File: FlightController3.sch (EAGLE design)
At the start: 27 parts, among them U1 NUCLEO_L432KC

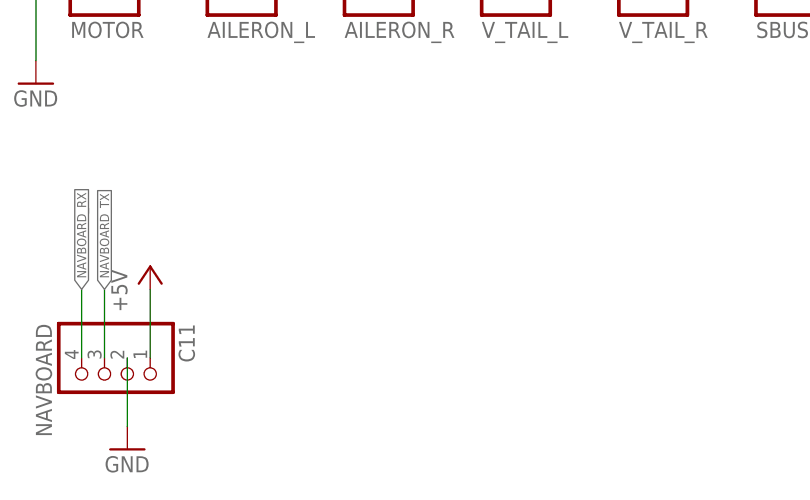
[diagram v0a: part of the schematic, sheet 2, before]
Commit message: added reset header
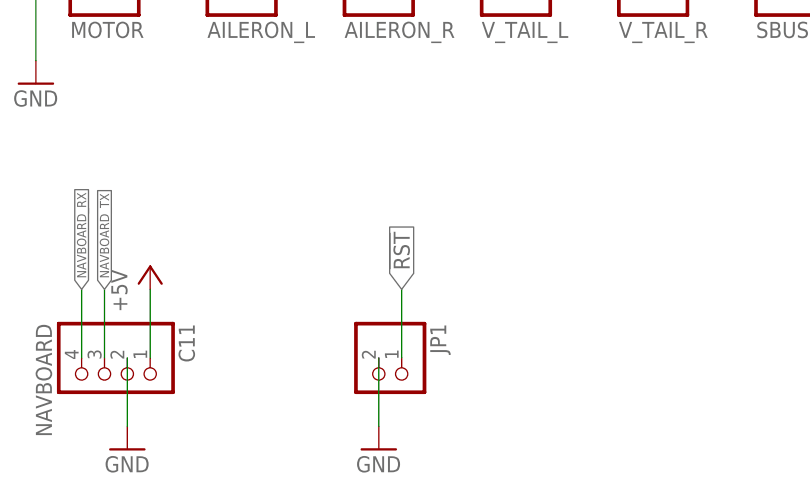
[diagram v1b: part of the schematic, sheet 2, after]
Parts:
- added JP1: (no value), pinhead:PINHD-1X2
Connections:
- new net !RST: JP1.1, U1.!RST
- net GND: now also JP1.2
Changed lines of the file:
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@@
 <part name="FRAME4" library="frames" deviceset="A4L-LOC" device=""/>
 <part name="U$1" library="toolbox" deviceset="TOOLBOX_LOGO" device=""/>
+<part name="JP1" library="pinhead" deviceset="PINHD-1X2" device=""/>
+<part name="GND8" library="supply1" deviceset="GND" device=""/>
 </parts>
 <sheets>
@@
 <wire x1="111.76" y1="116.84" x2="106.68" y2="116.84" width="0.1524" layer="91"/>
 <label x="106.68" y="116.84" size="1.778" layer="95" rot="R180" xref="yes"/>
+</segment>
+</net>
+<net name="!RST" class="0">
+<segment>
+<pinref part="U1" gate="G$1" pin="!RST"/>
+<wire x1="147.32" y1="76.2" x2="152.4" y2="76.2" width="0.1524" layer="91"/>
+<label x="152.4" y="76.2" size="1.778" layer="95" xref="yes"/>
 </segment>
 </net>
@@
 <instance part="C14" gate="A" x="218.44" y="114.3" rot="R270"/>
 <instance part="FRAME1" gate="G$1" x="0" y="0"/>
+<instance part="JP1" gate="G$1" x="58.42" y="81.28" rot="R270"/>
+<instance part="GND8" gate="1" x="58.42" y="73.66"/>
 </instances>
 <busses>
@@
 <junction x="220.98" y="129.54"/>
 </segment>
+<segment>
+<pinref part="JP1" gate="G$1" pin="2"/>
+<wire x1="58.42" y1="83.82" x2="58.42" y2="76.2" width="0.1524" layer="91"/>
+<pinref part="GND8" gate="1" pin="GND"/>
+</segment>
 </net>
 <net name="PPM_MOTOR" class="0">
@@
 </segment>
 </net>
+<net name="!RST" class="0">
+<segment>
+<pinref part="JP1" gate="G$1" pin="1"/>
+<wire x1="60.96" y1="83.82" x2="60.96" y2="91.44" width="0.1524" layer="91"/>
+<label x="60.96" y="91.44" size="1.778" layer="95" rot="R90" xref="yes"/>
+</segment>
+</net>

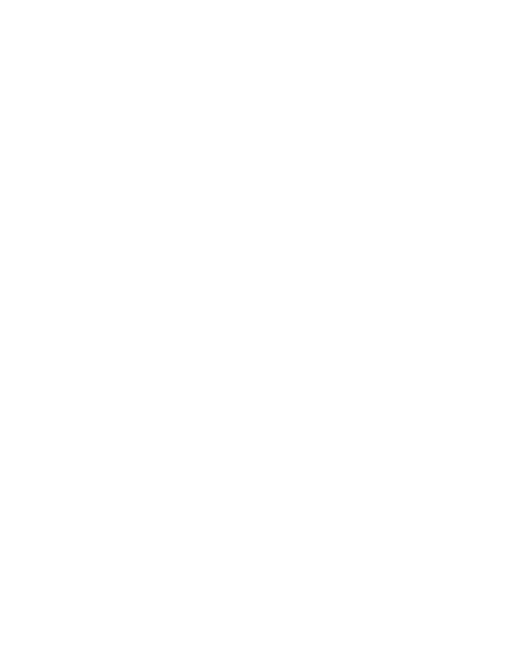
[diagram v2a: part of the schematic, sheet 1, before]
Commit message: power LEDs
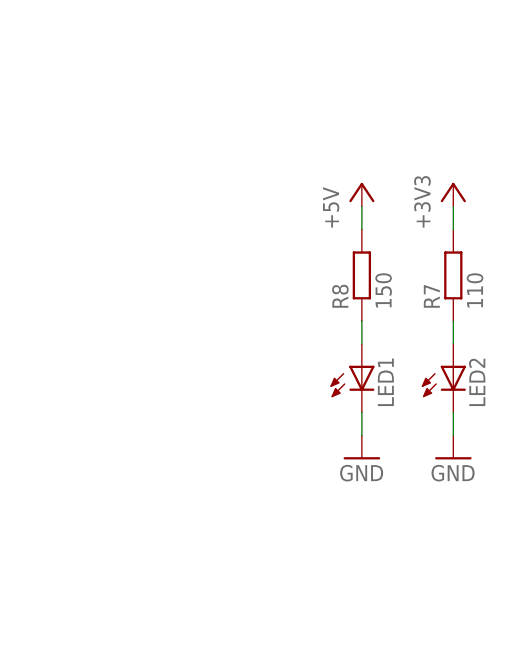
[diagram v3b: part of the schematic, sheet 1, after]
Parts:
- added LED1, LED2: (no value), led:LEDSML0603
- added R7: 110, resistor:R-EU_M1206
- added R8: 150, resistor:R-EU_M1206
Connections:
- new net N$2: LED2.A, R7.1
- new net N$3: LED1.A, R8.1
- net +3V3: now also R7.2
- net +5V: now also R8.2
- net GND: now also LED1.C, LED2.C
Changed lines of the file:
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@@
 <part name="JP1" library="pinhead" deviceset="PINHD-1X2" device=""/>
 <part name="GND8" library="supply1" deviceset="GND" device=""/>
+<part name="LED1" library="led" deviceset="LED" device="SML0603"/>
+<part name="LED2" library="led" deviceset="LED" device="SML0603"/>
+<part name="+3V2" library="supply1" deviceset="+3V3" device=""/>
+<part name="P+8" library="supply1" deviceset="+5V" device=""/>
+<part name="R7" library="resistor" deviceset="R-EU_" device="M1206" value="110"/>
+<part name="R8" library="resistor" deviceset="R-EU_" device="M1206" value="150"/>
+<part name="GND9" library="supply1" deviceset="GND" device=""/>
+<part name="GND10" library="supply1" deviceset="GND" device=""/>
 </parts>
 <sheets>
@@
 <instance part="FRAME2" gate="G$1" x="0" y="0"/>
 <instance part="U$1" gate="G$1" x="35.56" y="154.94"/>
+<instance part="LED1" gate="G$1" x="223.52" y="111.76"/>
+<instance part="LED2" gate="G$1" x="233.68" y="111.76"/>
+<instance part="+3V2" gate="G$1" x="233.68" y="132.08"/>
+<instance part="P+8" gate="1" x="223.52" y="132.08"/>
+<instance part="R7" gate="G$1" x="233.68" y="121.92" rot="R90"/>
+<instance part="R8" gate="G$1" x="223.52" y="121.92" rot="R90"/>
+<instance part="GND9" gate="1" x="223.52" y="101.6"/>
+<instance part="GND10" gate="1" x="233.68" y="101.6"/>
 </instances>
 <busses>
@@
 <pinref part="P+3" gate="1" pin="+5V"/>
 </segment>
+<segment>
+<pinref part="P+8" gate="1" pin="+5V"/>
+<pinref part="R8" gate="G$1" pin="2"/>
+<wire x1="223.52" y1="129.54" x2="223.52" y2="127" width="0.1524" layer="91"/>
+</segment>
 </net>
 <net name="GND" class="0">
@@
 <wire x1="104.14" y1="76.2" x2="104.14" y2="68.58" width="0.1524" layer="91"/>
 <pinref part="GND4" gate="1" pin="GND"/>
+</segment>
+<segment>
+<pinref part="LED2" gate="G$1" pin="C"/>
+<pinref part="GND10" gate="1" pin="GND"/>
+<wire x1="233.68" y1="106.68" x2="233.68" y2="104.14" width="0.1524" layer="91"/>
+</segment>
+<segment>
+<pinref part="LED1" gate="G$1" pin="C"/>
+<pinref part="GND9" gate="1" pin="GND"/>
+<wire x1="223.52" y1="106.68" x2="223.52" y2="104.14" width="0.1524" layer="91"/>
 </segment>
 </net>
@@
 <wire x1="162.56" y1="86.36" x2="162.56" y2="93.98" width="0.1524" layer="91"/>
 <pinref part="+3V1" gate="G$1" pin="+3V3"/>
+</segment>
+<segment>
+<pinref part="+3V2" gate="G$1" pin="+3V3"/>
+<pinref part="R7" gate="G$1" pin="2"/>
+<wire x1="233.68" y1="129.54" x2="233.68" y2="127" width="0.1524" layer="91"/>
 </segment>
 </net>
@@
 </segment>
 </net>
+<net name="N$2" class="0">
+<segment>
+<pinref part="R7" gate="G$1" pin="1"/>
+<pinref part="LED2" gate="G$1" pin="A"/>
+<wire x1="233.68" y1="116.84" x2="233.68" y2="114.3" width="0.1524" layer="91"/>
+</segment>
+</net>
+<net name="N$3" class="0">
+<segment>
+<pinref part="LED1" gate="G$1" pin="A"/>
+<pinref part="R8" gate="G$1" pin="1"/>
+<wire x1="223.52" y1="114.3" x2="223.52" y2="116.84" width="0.1524" layer="91"/>
+</segment>
+</net>

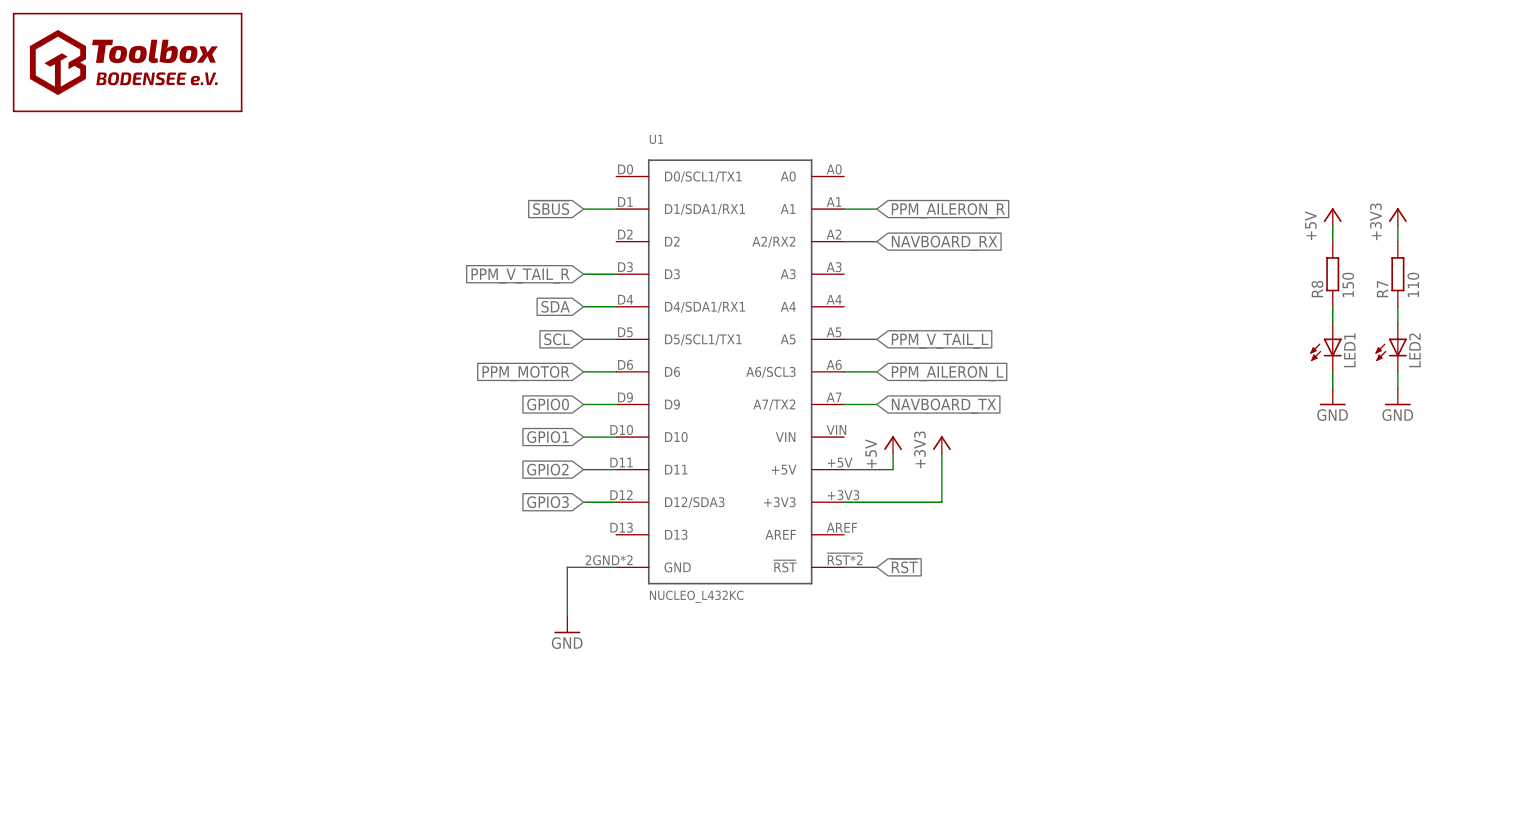
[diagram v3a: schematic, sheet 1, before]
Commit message: capacitors, dimensions, reset button
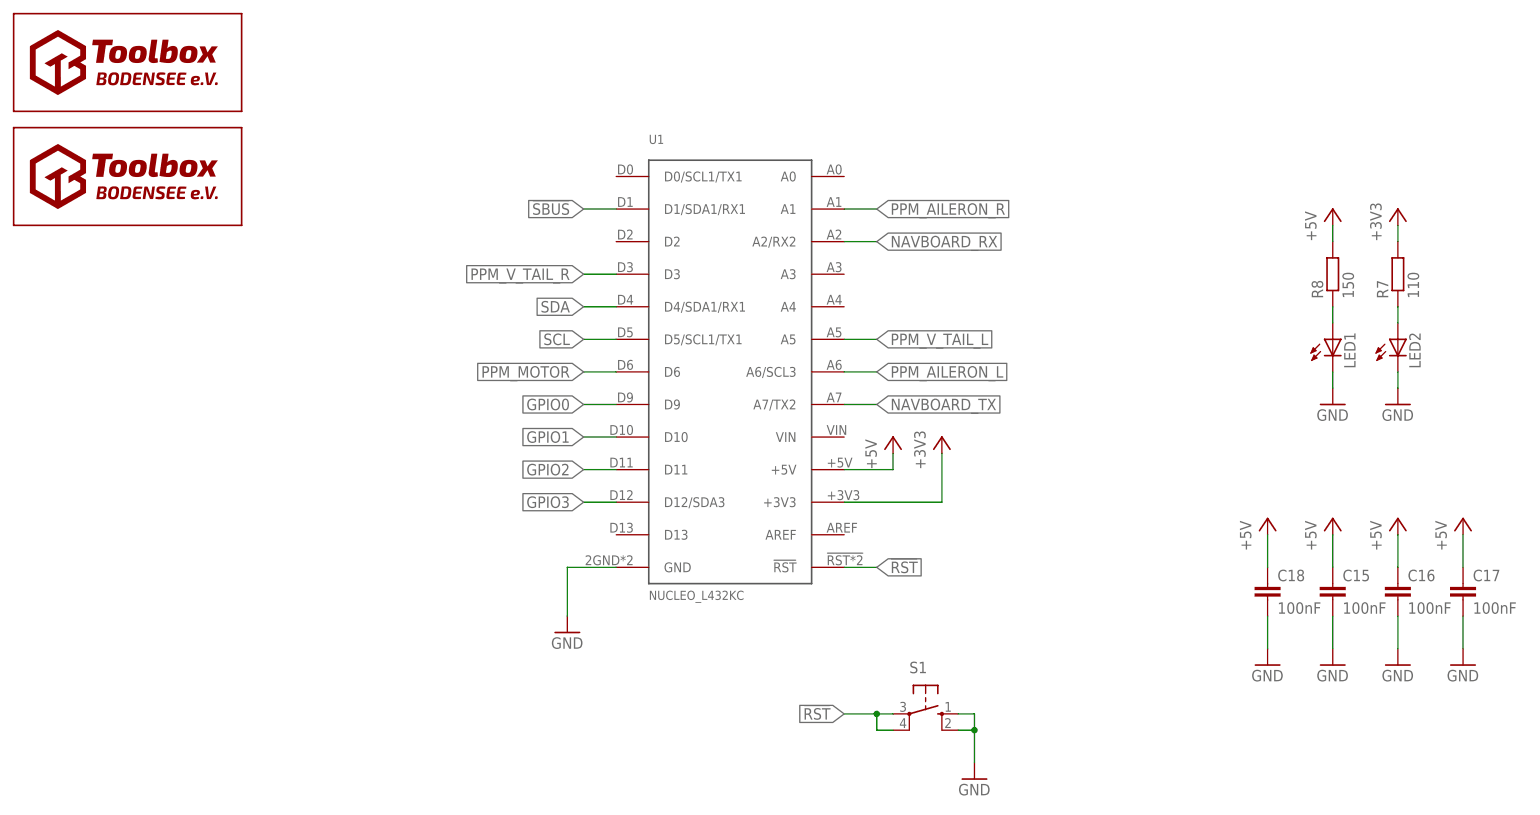
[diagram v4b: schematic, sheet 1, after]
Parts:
- added C15, C16, C17, C18: 100nF, resistor:C-EUC1206
- added S1: (no value), switch-omron:10-XX
- added U$2: TOOLBOX_LOGO, toolbox:TOOLBOX_LOGO
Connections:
- net !RST: now also S1.P, S1.P1
- net +5V: now also C15.1, C16.1, C17.1, C18.1
- net GND: now also C15.2, C16.2, C17.2, C18.2, S1.S, S1.S1
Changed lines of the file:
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@@
 <part name="GND9" library="supply1" deviceset="GND" device=""/>
 <part name="GND10" library="supply1" deviceset="GND" device=""/>
+<part name="C15" library="resistor" deviceset="C-EU" device="C1206" value="100nF"/>
+<part name="C16" library="resistor" deviceset="C-EU" device="C1206" value="100nF"/>
+<part name="C17" library="resistor" deviceset="C-EU" device="C1206" value="100nF"/>
+<part name="C18" library="resistor" deviceset="C-EU" device="C1206" value="100nF"/>
+<part name="P+10" library="supply1" deviceset="+5V" device=""/>
+<part name="P+11" library="supply1" deviceset="+5V" device=""/>
+<part name="P+12" library="supply1" deviceset="+5V" device=""/>
+<part name="P+13" library="supply1" deviceset="+5V" device=""/>
+<part name="GND12" library="supply1" deviceset="GND" device=""/>
+<part name="GND13" library="supply1" deviceset="GND" device=""/>
+<part name="GND14" library="supply1" deviceset="GND" device=""/>
+<part name="GND15" library="supply1" deviceset="GND" device=""/>
+<part name="S1" library="switch-omron" deviceset="10-XX" device=""/>
+<part name="GND11" library="supply1" deviceset="GND" device=""/>
+<part name="U$2" library="toolbox" deviceset="TOOLBOX_LOGO" device=""/>
 </parts>
 <sheets>
@@
 <instance part="GND9" gate="1" x="223.52" y="101.6"/>
 <instance part="GND10" gate="1" x="233.68" y="101.6"/>
+<instance part="C15" gate="G$1" x="223.52" y="73.66"/>
+<instance part="C16" gate="G$1" x="233.68" y="73.66"/>
+<instance part="C17" gate="G$1" x="243.84" y="73.66"/>
+<instance part="C18" gate="G$1" x="213.36" y="73.66"/>
+<instance part="P+10" gate="1" x="213.36" y="83.82"/>
+<instance part="P+11" gate="1" x="223.52" y="83.82"/>
+<instance part="P+12" gate="1" x="233.68" y="83.82"/>
+<instance part="P+13" gate="1" x="243.84" y="83.82"/>
+<instance part="GND12" gate="1" x="213.36" y="60.96"/>
+<instance part="GND13" gate="1" x="223.52" y="60.96"/>
+<instance part="GND14" gate="1" x="233.68" y="60.96"/>
+<instance part="GND15" gate="1" x="243.84" y="60.96"/>
+<instance part="S1" gate="1" x="160.02" y="53.34" rot="R270"/>
+<instance part="GND11" gate="1" x="167.64" y="43.18"/>
+<instance part="U$2" gate="G$1" x="35.56" y="137.16"/>
 </instances>
 <busses>
@@
 <wire x1="223.52" y1="129.54" x2="223.52" y2="127" width="0.1524" layer="91"/>
 </segment>
+<segment>
+<pinref part="P+10" gate="1" pin="+5V"/>
+<pinref part="C18" gate="G$1" pin="1"/>
+<wire x1="213.36" y1="81.28" x2="213.36" y2="76.2" width="0.1524" layer="91"/>
+</segment>
+<segment>
+<pinref part="C15" gate="G$1" pin="1"/>
+<pinref part="P+11" gate="1" pin="+5V"/>
+<wire x1="223.52" y1="76.2" x2="223.52" y2="81.28" width="0.1524" layer="91"/>
+</segment>
+<segment>
+<pinref part="P+12" gate="1" pin="+5V"/>
+<pinref part="C16" gate="G$1" pin="1"/>
+<wire x1="233.68" y1="81.28" x2="233.68" y2="76.2" width="0.1524" layer="91"/>
+</segment>
+<segment>
+<pinref part="C17" gate="G$1" pin="1"/>
+<pinref part="P+13" gate="1" pin="+5V"/>
+<wire x1="243.84" y1="76.2" x2="243.84" y2="81.28" width="0.1524" layer="91"/>
+</segment>
 </net>
 <net name="GND" class="0">
@@
 <wire x1="223.52" y1="106.68" x2="223.52" y2="104.14" width="0.1524" layer="91"/>
 </segment>
+<segment>
+<pinref part="C17" gate="G$1" pin="2"/>
+<pinref part="GND15" gate="1" pin="GND"/>
+<wire x1="243.84" y1="68.58" x2="243.84" y2="63.5" width="0.1524" layer="91"/>
+</segment>
+<segment>
+<pinref part="GND14" gate="1" pin="GND"/>
+<pinref part="C16" gate="G$1" pin="2"/>
+<wire x1="233.68" y1="63.5" x2="233.68" y2="68.58" width="0.1524" layer="91"/>
+</segment>
+<segment>
+<pinref part="C15" gate="G$1" pin="2"/>
+<pinref part="GND13" gate="1" pin="GND"/>
+<wire x1="223.52" y1="68.58" x2="223.52" y2="63.5" width="0.1524" layer="91"/>
+</segment>
+<segment>
+<pinref part="GND12" gate="1" pin="GND"/>
+<pinref part="C18" gate="G$1" pin="2"/>
+<wire x1="213.36" y1="63.5" x2="213.36" y2="68.58" width="0.1524" layer="91"/>
+</segment>
+<segment>
+<pinref part="S1" gate="1" pin="S1"/>
+<wire x1="165.1" y1="50.8" x2="167.64" y2="50.8" width="0.1524" layer="91"/>
+<wire x1="167.64" y1="50.8" x2="167.64" y2="45.72" width="0.1524" layer="91"/>
+<pinref part="S1" gate="1" pin="S"/>
+<wire x1="165.1" y1="53.34" x2="167.64" y2="53.34" width="0.1524" layer="91"/>
+<wire x1="167.64" y1="53.34" x2="167.64" y2="50.8" width="0.1524" layer="91"/>
+<junction x="167.64" y="50.8"/>
+<pinref part="GND11" gate="1" pin="GND"/>
+</segment>
 </net>
 <net name="PPM_MOTOR" class="0">
@@
 <label x="152.4" y="76.2" size="1.778" layer="95" xref="yes"/>
 </segment>
-</net>
+<segment>
+<pinref part="S1" gate="1" pin="P"/>
+<wire x1="154.94" y1="53.34" x2="152.4" y2="53.34" width="0.1524" layer="91"/>
+<pinref part="S1" gate="1" pin="P1"/>
+<wire x1="152.4" y1="53.34" x2="147.32" y2="53.34" width="0.1524" layer="91"/>
+<wire x1="154.94" y1="50.8" x2="152.4" y2="50.8" width="0.1524" layer="91"/>
+<wire x1="152.4" y1="50.8" x2="152.4" y2="53.34" width="0.1524" layer="91"/>
+<junction x="152.4" y="53.34"/>
+<label x="147.32" y="53.34" size="1.778" layer="95" rot="R180" xref="yes"/>
+</segment>
+</net>
